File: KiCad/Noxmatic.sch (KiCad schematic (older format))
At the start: 22 parts, among them Q1 IRF3708, Q2 IRF3708, U1 NodeMCU_Amica_R2, U2 DS18B20

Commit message: Schaltplan fix
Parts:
- added R?: 47, symbol R
- L1: value Drossel 15mH -> Drossel 47uH >200mA
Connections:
- wire segments 89 -> 93
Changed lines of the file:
@@
 	0    1    1    0
 $EndComp
-Wire Wire Line
-	4450 4800 4450 4650
-Wire Wire Line
-	4450 5450 4450 5300
-Wire Wire Line
-	4850 4800 4750 4800
-Wire Wire Line
-	4850 5900 4850 5450
-Wire Wire Line
-	4850 5450 4850 4800
 $Comp
 L DS18B20 U2
@@
 	1    0    0    -1
 $EndComp
-Connection ~ 4850 4800
 $Comp
 L R R1
@@
 P 1100 5400
 F 0 "L1" V 1050 5400 50  0000 C CNN
-F 1 "Drossel 15mH" V 1150 5800 50  0000 C CNN
+F 1 "Drossel 47uH >200mA" V 1150 5950 50  0000 C CNN
 F 2 "" H 1100 5400 50  0000 C CNN
 F 3 "" H 1100 5400 50  0000 C CNN
@@
 	-1   0    0    1
 $EndComp
-Wire Wire Line
-	1100 5550 1400 5550
 $Comp
 L GND #PWR1
@@
 	1    0    0    -1
 $EndComp
-Wire Wire Line
-	800  5550 800  5900
-Wire Wire Line
-	800  5900 3450 5900
-Wire Wire Line
-	3450 5900 4850 5900
-Connection ~ 4850 5450
-Wire Wire Line
-	3750 5600 3450 5600
-Wire Wire Line
-	3750 5900 3750 5900
-Wire Wire Line
-	5600 5350 5600 6000
-Wire Wire Line
-	1100 5250 750  5250
-Wire Wire Line
-	750  5250 750  6000
-Wire Wire Line
-	750  6000 5600 6000
-Wire Wire Line
-	4750 5450 4850 5450
-Wire Wire Line
-	4850 5450 5500 5450
-Wire Wire Line
-	6900 5150 6300 5150
-Wire Wire Line
-	6300 5150 5600 5150
-Wire Wire Line
-	5600 5150 5500 5150
-Wire Wire Line
-	5450 4350 5600 4350
-Wire Wire Line
-	6900 4250 6550 4250
-Wire Wire Line
-	6900 4350 6900 4450
-Wire Wire Line
-	6900 4450 6900 5150
-Wire Wire Line
-	6900 4450 7200 4450
-Wire Wire Line
-	7200 4450 7200 4050
-Wire Wire Line
-	7200 4050 6900 4050
-Wire Wire Line
-	6900 4050 6900 4150
-Connection ~ 6300 5150
-Connection ~ 6900 4450
 Text Notes 5900 4150 0    60   ~ 0
 Temperature
@@
 Text Notes 5950 5200 0    60   ~ 0
 GND
-Wire Wire Line
-	6500 5350 5600 5350
-Wire Wire Line
-	5500 5150 5500 5450
-Connection ~ 5600 5150
-Connection ~ 5600 5350
-Wire Wire Line
-	4050 5600 5400 5600
-Wire Wire Line
-	5400 5600 5400 4950
-Wire Wire Line
-	5400 4950 5600 4950
-Wire Wire Line
-	4750 5050 5300 5050
-Wire Wire Line
-	5300 5050 5300 4750
-Wire Wire Line
-	5300 4750 5600 4750
-Wire Wire Line
-	4750 4400 5300 4400
-Wire Wire Line
-	5300 4400 5300 4550
-Wire Wire Line
-	5300 4550 5600 4550
-Connection ~ 3750 5600
-Connection ~ 3450 5600
-Connection ~ 3450 5900
-Connection ~ 5600 4350
-Connection ~ 5600 4550
-Connection ~ 5600 4750
-Connection ~ 5600 4950
 $Comp
 L DOGS102-6 DS?
@@
 	0    1    1    0
 $EndComp
-Wire Wire Line
-	4450 4150 4450 4000
 $Comp
 L Screw_Terminal_1x07 J?
@@
 	-1   0    0    1
 $EndComp
-Wire Wire Line
-	2300 4450 4150 4450
-Wire Wire Line
-	4150 4450 4150 4000
-Wire Wire Line
-	2300 4550 4150 4550
-Wire Wire Line
-	4150 4550 4150 4650
-Wire Wire Line
-	2300 4850 3400 4850
-Wire Wire Line
-	3400 4850 3400 3350
-Wire Wire Line
-	3400 3350 5400 3350
-Wire Wire Line
-	5400 3350 5400 2850
-Wire Wire Line
-	2300 5050 3300 5050
-Wire Wire Line
-	3300 5050 3300 3250
-Wire Wire Line
-	3300 3250 5300 3250
-Wire Wire Line
-	5300 3250 5300 2850
 $Comp
 L R R?
@@
 	0    -1   -1   0
 $EndComp
+Text Notes 5950 4400 0    60   ~ 0
+Heatgrip (L)
+Wire Wire Line
+	4450 4800 4450 4650
+Wire Wire Line
+	4450 5450 4450 5300
+Wire Wire Line
+	4850 4800 4750 4800
+Wire Wire Line
+	4850 5900 4850 4800
+Connection ~ 4850 4800
+Wire Wire Line
+	1100 5550 1400 5550
+Wire Wire Line
+	800  5550 800  5900
+Wire Wire Line
+	800  5900 4850 5900
+Connection ~ 4850 5450
+Wire Wire Line
+	3750 5600 3450 5600
+Wire Wire Line
+	3750 5900 3750 5900
+Wire Wire Line
+	5600 5350 5600 6000
+Wire Wire Line
+	1100 5250 750  5250
+Wire Wire Line
+	750  5250 750  6000
+Wire Wire Line
+	750  6000 5600 6000
+Wire Wire Line
+	4750 5450 5500 5450
+Wire Wire Line
+	6900 5150 5500 5150
+Wire Wire Line
+	5450 4350 5600 4350
+Wire Wire Line
+	6900 4250 6550 4250
+Wire Wire Line
+	6900 4350 6900 5150
+Wire Wire Line
+	6900 4450 7200 4450
+Wire Wire Line
+	7200 4450 7200 4050
+Wire Wire Line
+	7200 4050 6900 4050
+Wire Wire Line
+	6900 4050 6900 4150
+Connection ~ 6300 5150
+Connection ~ 6900 4450
+Wire Wire Line
+	6500 5350 5600 5350
+Wire Wire Line
+	5500 5150 5500 5450
+Connection ~ 5600 5150
+Connection ~ 5600 5350
+Wire Wire Line
+	4050 5600 5400 5600
+Wire Wire Line
+	5400 5600 5400 4950
+Wire Wire Line
+	5400 4950 5600 4950
+Wire Wire Line
+	4750 5050 5300 5050
+Wire Wire Line
+	5300 5050 5300 4750
+Wire Wire Line
+	5300 4750 5600 4750
+Wire Wire Line
+	4750 4400 5300 4400
+Wire Wire Line
+	5300 4400 5300 4550
+Wire Wire Line
+	5300 4550 5600 4550
+Connection ~ 3750 5600
+Connection ~ 3450 5600
+Connection ~ 3450 5900
+Connection ~ 5600 4350
+Connection ~ 5600 4550
+Connection ~ 5600 4750
+Connection ~ 5600 4950
+Wire Wire Line
+	4450 4150 4450 4000
+Wire Wire Line
+	2300 4450 4150 4450
+Wire Wire Line
+	4150 4450 4150 4000
+Wire Wire Line
+	2300 4550 4150 4550
+Wire Wire Line
+	4150 4550 4150 4650
+Wire Wire Line
+	2300 4850 3400 4850
+Wire Wire Line
+	3400 4850 3400 3350
+Wire Wire Line
+	3400 3350 5400 3350
+Wire Wire Line
+	5400 3350 5400 2850
+Wire Wire Line
+	2300 5050 3300 5050
+Wire Wire Line
+	3300 5050 3300 3250
+Wire Wire Line
+	3300 3250 5300 3250
+Wire Wire Line
+	5300 3250 5300 2850
 Wire Wire Line
 	6200 2350 6200 2450
@@
 	6200 1850 4050 1850
 Wire Wire Line
-	4050 1850 4050 2400
-Wire Wire Line
-	4050 2400 4600 2400
+	4050 1850 4050 3000
+Wire Wire Line
+	2850 2400 4600 2400
 Wire Wire Line
 	4600 2400 4600 2300
 Wire Wire Line
-	5800 3150 4300 3150
+	3100 3150 5800 3150
 Wire Wire Line
 	4300 3150 4300 2100
@@
 	2600 4650 2600 4350
 Wire Wire Line
-	2300 4350 2600 4350
-Wire Wire Line
-	2600 4350 3000 4350
+	2300 4350 3000 4350
 Wire Wire Line
 	3000 4350 3000 3650
@@
 Wire Wire Line
 	6550 4150 5600 4150
-Text Notes 5950 4400 0    60   ~ 0
-Heatgrip (L)
 Wire Wire Line
 	4150 5300 4150 4950
@@
 Wire Wire Line
 	3450 5150 3450 5600
+Wire Wire Line
+	1400 5450 1350 5450
+Wire Wire Line
+	1350 5450 1350 5900
+Connection ~ 1350 5900
+$Comp
+L R R?
+U 1 1 58F7C162
+P 4650 2850
+F 0 "R?" V 4730 2850 50  0000 C CNN
+F 1 "47" V 4650 2850 50  0000 C CNN
+F 2 "" V 4580 2850 50  0000 C CNN
+F 3 "" H 4650 2850 50  0000 C CNN
+	1    4650 2850
+	0    1    1    0
+$EndComp
+Wire Wire Line
+	4800 2850 4900 2850
+Wire Wire Line
+	4500 2850 4500 3150
+Connection ~ 4500 3150
+Wire Wire Line
+	5000 2850 5100 2850
+Wire Wire Line
+	5000 2850 5000 3000
+Wire Wire Line
+	5000 3000 4050 3000
+Connection ~ 4050 2400
+Wire Wire Line
+	2300 5550 3100 5550
+Wire Wire Line
+	3100 5550 3100 3150
+Connection ~ 4300 3150
+Wire Wire Line
+	2300 5450 2850 5450
+Wire Wire Line
+	2850 5450 2850 2400
 $EndSCHEMATC

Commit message: korrektur
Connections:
- wire segments 93 -> 94
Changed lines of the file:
@@
 Heatgrip (L)
-Wire Wire Line
-	4450 4800 4450 4650
-Wire Wire Line
-	4450 5450 4450 5300
 Wire Wire Line
 	4850 4800 4750 4800
@@
 	2300 4550 4150 4550
 Wire Wire Line
-	4150 4550 4150 4650
+	4150 4550 4150 4800
 Wire Wire Line
 	2300 4850 3400 4850
@@
 	6550 4150 5600 4150
 Wire Wire Line
-	4150 5300 4150 4950
+	4150 4950 4150 5450
 Wire Wire Line
 	4150 4950 2300 4950
@@
 Wire Wire Line
 	2850 5450 2850 2400
+Wire Wire Line
+	4150 5450 4450 5450
+Connection ~ 4150 5300
+Wire Wire Line
+	4150 4800 4450 4800
+Connection ~ 4150 4650
+Wire Wire Line
+	4450 4150 4150 4150
+Connection ~ 4150 4150
 $EndSCHEMATC

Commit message: Anpassung des Pullup für den DS18B20 (läuft sonst auf NodeMcu nicht)
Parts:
- R1: value 4,7k -> 1k
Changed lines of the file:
@@
 P 2450 4650
 F 0 "R1" V 2530 4650 50  0000 C CNN
-F 1 "4,7k" V 2450 4650 50  0000 C CNN
+F 1 "1k" V 2450 4650 50  0000 C CNN
 F 2 "" V 2380 4650 50  0000 C CNN
 F 3 "" H 2450 4650 50  0000 C CNN

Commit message: Fix Reboots durch Interrupt + Widerstand am Display festgelegt
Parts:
- R8: renamed from R?; value 47 -> 1k
- gave numbers to parts that had none: 9
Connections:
- wire segments 94 -> 93
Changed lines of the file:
@@
 LIBS:valves
 LIBS:nodemcu
-LIBS:DS18B20
 LIBS:displays
+LIBS:maxim
 LIBS:Noxmatic-cache
 EELAYER 25 0
@@
 $EndComp
 $Comp
-L DS18B20 U2
-U 1 1 58F5289F
-P 7050 4250
-F 0 "U2" H 7050 4150 50  0000 C CNN
-F 1 "DS18B20" H 7450 4350 50  0000 C CNN
-F 2 "MODULE" H 7050 4250 50  0001 C CNN
-F 3 "DOCUMENTATION" H 7050 4250 50  0001 C CNN
-	1    7050 4250
-	1    0    0    -1
-$EndComp
-$Comp
 L R R1
 U 1 1 58F5563D
@@
 GND
 $Comp
-L DOGS102-6 DS?
+L DOGS102-6 DS1
 U 1 1 58F67BBD
 P 5300 2400
-F 0 "DS?" H 4750 2800 40  0000 C CNN
+F 0 "DS1" H 4750 2800 40  0000 C CNN
 F 1 "DOGS102-6" H 5300 2400 40  0000 C CNN
 F 2 "" H 5300 2400 60  0000 C CNN
@@
 $EndComp
 $Comp
-L IRLB8721PBF Q?
+L IRLB8721PBF Q3
 U 1 1 58F6C11E
 P 4650 3950
-F 0 "Q?" H 4900 4025 50  0000 L CNN
+F 0 "Q3" H 4900 4025 50  0000 L CNN
 F 1 "IRF3708" H 4900 3950 50  0000 L CNN
 F 2 "TO_SOT_Packages_THT:TO-220_Neutral123_Vertical" H 4900 3875 50  0001 L CIN
@@
 $EndComp
 $Comp
-L R R?
+L R R7
 U 1 1 58F6C124
 P 4600 4150
-F 0 "R?" V 4680 4150 50  0000 C CNN
+F 0 "R7" V 4680 4150 50  0000 C CNN
 F 1 "10k" V 4600 4150 50  0000 C CNN
 F 2 "" V 4530 4150 50  0000 C CNN
@@
 $EndComp
 $Comp
-L R R?
+L R R6
 U 1 1 58F6C12A
 P 4300 4000
-F 0 "R?" V 4380 4000 50  0000 C CNN
+F 0 "R6" V 4380 4000 50  0000 C CNN
 F 1 "100" V 4300 4000 50  0000 C CNN
 F 2 "" V 4230 4000 50  0000 C CNN
@@
 $EndComp
 $Comp
-L Screw_Terminal_1x07 J?
+L Screw_Terminal_1x07 J1
 U 1 1 58F6C246
 P 5800 4750
-F 0 "J?" H 5800 5500 50  0000 C TNN
+F 0 "J1" H 5800 5500 50  0000 C TNN
 F 1 "Screw_Terminal_1x07" V 5650 4750 50  0000 C TNN
 F 2 "" H 5800 4025 50  0001 C CNN
@@
 $EndComp
 $Comp
-L R R?
+L R R9
 U 1 1 58F6E36A
 P 5800 3000
-F 0 "R?" V 5880 3000 50  0000 C CNN
+F 0 "R9" V 5880 3000 50  0000 C CNN
 F 1 "10k" V 5800 3000 50  0000 C CNN
 F 2 "" V 5730 3000 50  0000 C CNN
@@
 $EndComp
 $Comp
-L C_Small C?
+L C_Small C2
 U 1 1 58F6ED87
 P 6100 2100
-F 0 "C?" H 6110 2170 50  0000 L CNN
+F 0 "C2" H 6110 2170 50  0000 L CNN
 F 1 "1uF" H 5950 2000 50  0000 L CNN
 F 2 "" H 6100 2100 50  0000 C CNN
@@
 $EndComp
 $Comp
-L C_Small C?
+L C_Small C4
 U 1 1 58F70269
 P 6450 2400
-F 0 "C?" H 6460 2470 50  0000 L CNN
+F 0 "C4" H 6460 2470 50  0000 L CNN
 F 1 "1uF" H 6300 2300 50  0000 L CNN
 F 2 "" H 6450 2400 50  0000 C CNN
@@
 $EndComp
 $Comp
-L C_Small C?
+L C_Small C3
 U 1 1 58F70366
 P 6100 2350
-F 0 "C?" H 6110 2420 50  0000 L CNN
+F 0 "C3" H 6110 2420 50  0000 L CNN
 F 1 "1uF" H 5950 2250 50  0000 L CNN
 F 2 "" H 6100 2350 50  0000 C CNN
@@
 Wire Wire Line
 	6900 4350 6900 5150
-Wire Wire Line
-	6900 4450 7200 4450
-Wire Wire Line
-	7200 4450 7200 4050
-Wire Wire Line
-	7200 4050 6900 4050
-Wire Wire Line
-	6900 4050 6900 4150
 Connection ~ 6300 5150
-Connection ~ 6900 4450
 Wire Wire Line
 	6500 5350 5600 5350
 Wire Wire Line
-	5500 5150 5500 5450
+	5500 5450 5500 5150
 Connection ~ 5600 5150
 Connection ~ 5600 5350
@@
 Wire Wire Line
 	5300 4550 5600 4550
-Connection ~ 3750 5600
 Connection ~ 3450 5600
 Connection ~ 3450 5900
@@
 	4450 4150 4450 4000
 Wire Wire Line
-	2300 4450 4150 4450
-Wire Wire Line
-	4150 4450 4150 4000
+	4150 4450 2300 4450
+Wire Wire Line
+	4150 4000 4150 4450
 Wire Wire Line
 	2300 4550 4150 4550
@@
 	4050 1850 4050 3000
 Wire Wire Line
-	2850 2400 4600 2400
+	1350 2400 4600 2400
 Wire Wire Line
 	4600 2400 4600 2300
 Wire Wire Line
-	3100 3150 5800 3150
+	4300 3150 5800 3150
 Wire Wire Line
 	4300 3150 4300 2100
 Wire Wire Line
-	4300 2100 4600 2100
+	1250 2100 4600 2100
 Wire Wire Line
 	4600 2100 4600 2200
@@
 	6550 4150 5600 4150
 Wire Wire Line
-	4150 4950 4150 5450
-Wire Wire Line
-	4150 4950 2300 4950
-Wire Wire Line
-	2300 5150 3450 5150
-Wire Wire Line
-	3450 5150 3450 5600
-Wire Wire Line
 	1400 5450 1350 5450
 Wire Wire Line
@@
 Connection ~ 1350 5900
 $Comp
-L R R?
+L R R8
 U 1 1 58F7C162
 P 4650 2850
-F 0 "R?" V 4730 2850 50  0000 C CNN
-F 1 "47" V 4650 2850 50  0000 C CNN
+F 0 "R8" V 4730 2850 50  0000 C CNN
+F 1 "1k" V 4650 2850 50  0000 C CNN
 F 2 "" V 4580 2850 50  0000 C CNN
 F 3 "" H 4650 2850 50  0000 C CNN
@@
 	5000 3000 4050 3000
 Connection ~ 4050 2400
-Wire Wire Line
-	2300 5550 3100 5550
-Wire Wire Line
-	3100 5550 3100 3150
 Connection ~ 4300 3150
-Wire Wire Line
-	2300 5450 2850 5450
-Wire Wire Line
-	2850 5450 2850 2400
 Wire Wire Line
 	4150 5450 4450 5450
@@
 	4450 4150 4150 4150
 Connection ~ 4150 4150
+Wire Wire Line
+	2300 5150 4150 5150
+Wire Wire Line
+	4150 5150 4150 5450
+Wire Wire Line
+	2300 4950 3450 4950
+Wire Wire Line
+	3450 4950 3450 5600
+Wire Wire Line
+	1400 5050 1350 5050
+Wire Wire Line
+	1350 5050 1350 2400
+Wire Wire Line
+	1250 5150 1400 5150
+Wire Wire Line
+	1250 2100 1250 5150
+Connection ~ 4300 2100
+$Comp
+L DS18B20 U2
+U 1 1 5904F10D
+P 7200 4250
+F 0 "U2" H 7200 4150 50  0000 C CNN
+F 1 "DS18B20" H 7200 4500 50  0000 C CNN
+F 2 "MODULE" H 7200 4250 50  0001 C CNN
+F 3 "DOCUMENTATION" H 7200 4250 50  0001 C CNN
+	1    7200 4250
+	1    0    0    -1
+$EndComp
+Wire Wire Line
+	6900 4150 6700 4150
+Wire Wire Line
+	6700 4150 6700 4350
+Wire Wire Line
+	6700 4350 6900 4350
+Connection ~ 6900 4350
+Connection ~ 6900 4150
+Connection ~ 6900 4250
 $EndSCHEMATC

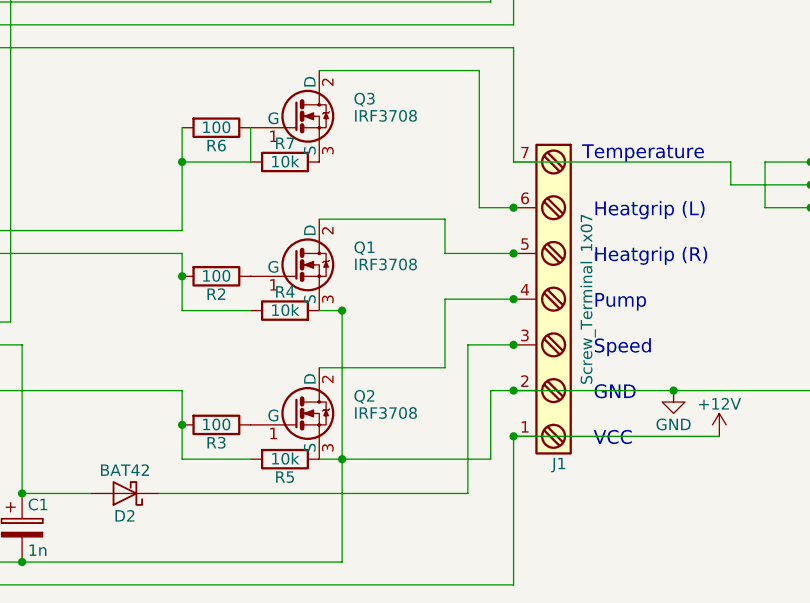
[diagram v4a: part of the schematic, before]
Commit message: Schaltplan korrektur
Fehlende Masseleitung eingefügt. PDF durch PNG ersetzt
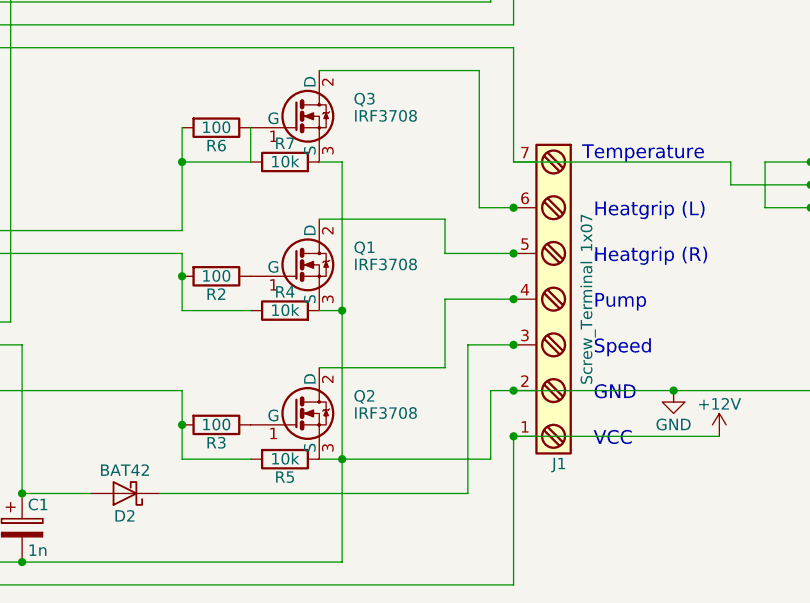
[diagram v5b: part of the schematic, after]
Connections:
- net GND: now also Q3.3 (S), R7.2
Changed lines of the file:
@@
 	4850 4800 4750 4800
 Wire Wire Line
-	4850 5900 4850 4800
+	4850 4150 4850 5900
 Connection ~ 4850 4800
 Wire Wire Line
@@
 	6500 5350 5600 5350
 Wire Wire Line
-	5500 5450 5500 5150
+	5500 5150 5500 5450
 Connection ~ 5600 5150
 Connection ~ 5600 5350
@@
 Connection ~ 6900 4150
 Connection ~ 6900 4250
+Wire Wire Line
+	4850 4150 4750 4150
 $EndSCHEMATC
